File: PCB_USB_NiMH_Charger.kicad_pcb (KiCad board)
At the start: 2 copper layers, 94.9 x 72 mm, 61 parts, among them J1 USB_C_Receptacle_Simple, J2 Conn_02x01, Q1 2SA1015, Q2 2SC2458, Q3 2SB834, Q4 2SC2458, Q5 2SB834, Q6 2SC2458, Q7 2SB834, Q8 2SC2458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

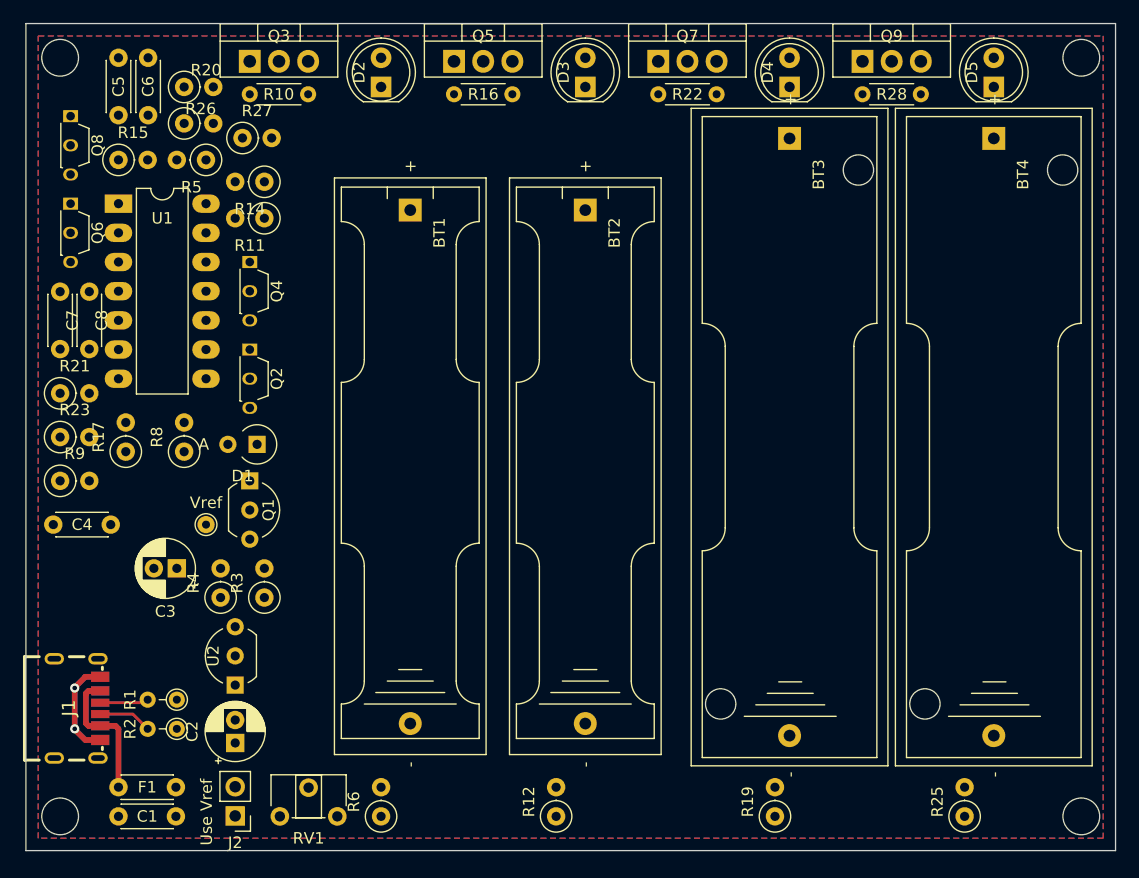
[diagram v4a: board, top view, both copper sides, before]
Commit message: Update to rev. 3
* LED を低消費電力版に変更し、LM339 で直接駆動するように変更。
  - 2SC1815 (2SC2458) を削除。
  - プルアップ抵抗を削除。
  - 680Ω を 2KΩ に変更。
* 10μF 電解コンデンサーを積層セラミックコンデンサーに変更。
* 2SB834 を裏面に配置。
* USB コネクタのフットプリントに間違いがあったのを修正。
  (取り付け穴が空いていなかったのを修正。)
* 配線を完了。
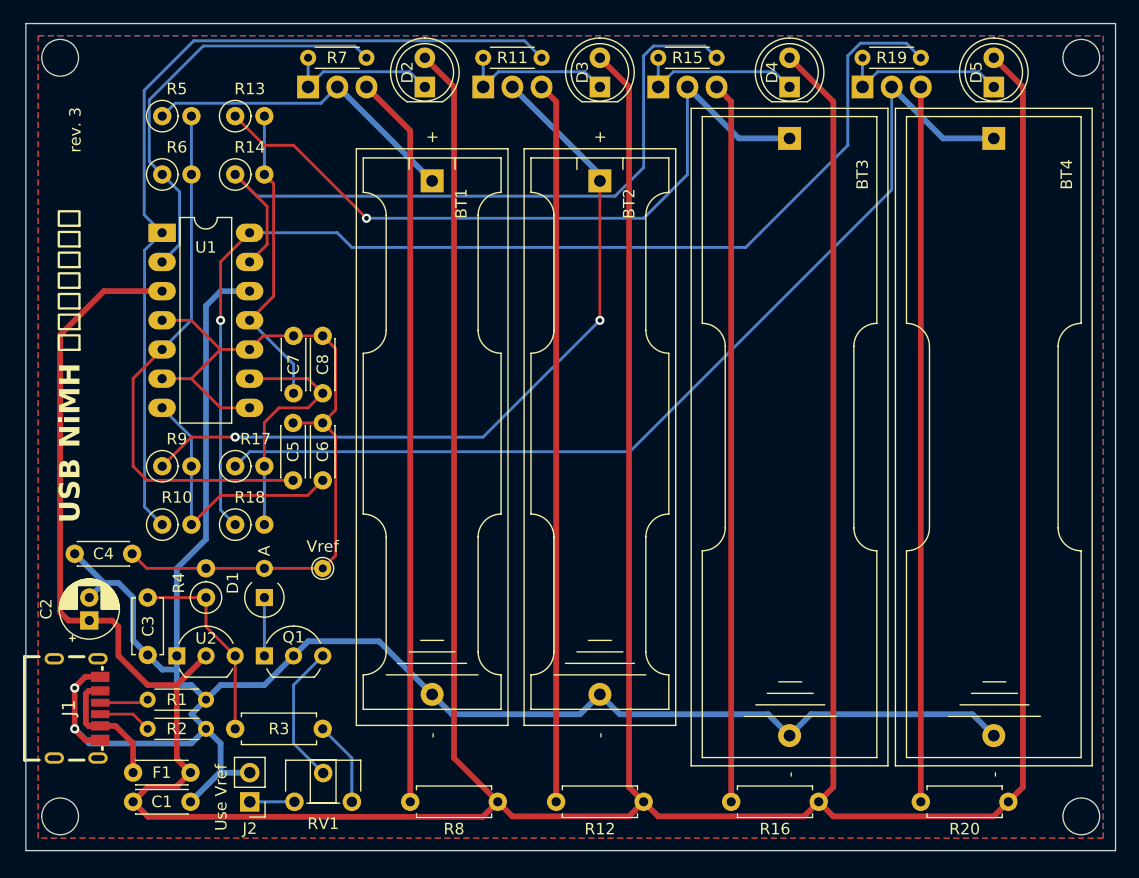
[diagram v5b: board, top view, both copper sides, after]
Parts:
- removed the Q2 at (44.5, 83.8)
- removed the Q4 at (44.5, 76.2)
- removed Q6, Q8: 2SC2458, Package_TO_SOT_THT:TO-92S_Wide
- removed the R11 at (45.7, 72.4)
- removed the R15 at (33.0, 67.3)
- removed the R20 at (38.7, 61.0)
- removed R21, R23, R27: 10k, Resistor_THT:R_Axial_DIN0207_L6.3mm_D2.5mm_P2.54mm_Vertical
- removed R26: 1M, Resistor_THT:R_Axial_DIN0207_L6.3mm_D2.5mm_P2.54mm_Vertical
- removed the R8 at (38.7, 92.7)
- added R13: 10k, Resistor_THT:R_Axial_DIN0207_L6.3mm_D2.5mm_P2.54mm_Vertical, F.Cu at (43.2, 63.5)
- added R14: 1M, Resistor_THT:R_Axial_DIN0207_L6.3mm_D2.5mm_P2.54mm_Vertical, F.Cu at (43.2, 68.6)
- added R18: 1M, Resistor_THT:R_Axial_DIN0207_L6.3mm_D2.5mm_P2.54mm_Vertical, F.Cu at (43.2, 99.1)
- added R6: 1M, Resistor_THT:R_Axial_DIN0207_L6.3mm_D2.5mm_P2.54mm_Vertical, F.Cu at (36.8, 68.6)
- C3: footprint Capacitor_THT:CP_Radial_D5.0mm_P2.00mm -> Capacitor_THT:C_Disc_D4.7mm_W2.5mm_P5.00mm
- D1: value 11EQS04 -> 11EQS03L
- Q2: renamed from Q3; footprint Package_TO_SOT_THT:TO-220-3_Vertical -> Package_TO_SOT_THT:TO-220-3_Horizontal_TabDown; moved to B.Cu
- Q3: renamed from Q5; footprint Package_TO_SOT_THT:TO-220-3_Vertical -> Package_TO_SOT_THT:TO-220-3_Horizontal_TabDown; moved to B.Cu
- Q4: renamed from Q7; footprint Package_TO_SOT_THT:TO-220-3_Vertical -> Package_TO_SOT_THT:TO-220-3_Horizontal_TabDown; moved to B.Cu
- Q5: renamed from Q9; footprint Package_TO_SOT_THT:TO-220-3_Vertical -> Package_TO_SOT_THT:TO-220-3_Horizontal_TabDown; moved to B.Cu
- R1, R2: footprint Resistor_THT:R_Axial_DIN0204_L3.6mm_D1.6mm_P2.54mm_Vertical -> Resistor_THT:R_Axial_DIN0204_L3.6mm_D1.6mm_P5.08mm_Horizontal
- R11: renamed from R16; value 680 -> 2.2k
- R12, R3: footprint Resistor_THT:R_Axial_DIN0207_L6.3mm_D2.5mm_P2.54mm_Vertical -> Resistor_THT:R_Axial_DIN0207_L6.3mm_D2.5mm_P7.62mm_Horizontal
- R15: renamed from R22; value 680 -> 2.2k
- R16: renamed from R19; value 10 -> 5.6; footprint Resistor_THT:R_Axial_DIN0207_L6.3mm_D2.5mm_P2.54mm_Vertical -> Resistor_THT:R_Axial_DIN0207_L6.3mm_D2.5mm_P7.62mm_Horizontal
- R19: renamed from R28; value 680 -> 2.2k
- R20: renamed from R25; value 10 -> 5.6; footprint Resistor_THT:R_Axial_DIN0207_L6.3mm_D2.5mm_P2.54mm_Vertical -> Resistor_THT:R_Axial_DIN0207_L6.3mm_D2.5mm_P7.62mm_Horizontal
- R7: renamed from R10; value 680 -> 2.2k
- R8: renamed from R6; footprint Resistor_THT:R_Axial_DIN0207_L6.3mm_D2.5mm_P2.54mm_Vertical -> Resistor_THT:R_Axial_DIN0207_L6.3mm_D2.5mm_P7.62mm_Horizontal
- moved C5 35.2 mm to (48.2, 95.2)
- moved C6 35.2 mm to (50.8, 95.2)
- moved R10 31.1 mm to (36.8, 99.1), turned to 0 degrees
- moved C7 20.7 mm to (48.3, 87.6)
- moved C8 20.7 mm to (50.8, 87.6)
- moved C2 16.6 mm to (30.5, 107.4)
- moved Q1 15.3 mm to (45.7, 110.5), turned to 0 degrees
- moved D1 13.4 mm to (45.7, 105.4), turned to 90 degrees
- moved R3 12.5 mm to (50.8, 116.8), turned to 180 degrees
- moved TP1 10.9 mm to (50.8, 102.9)
- moved R8 10.2 mm to (66.0, 123.2), turned to 180 degrees
- moved R17 9.61 mm to (43.2, 94.0), turned to 0 degrees
- moved R9 8.98 mm to (36.8, 94.0)
- moved R12 7.73 mm to (78.7, 123.2), turned to 180 degrees
- moved R7 5.99 mm to (49.5, 58.4)
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- renumbered R14 to R10
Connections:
- C5 pad 1: Net-(U1A--) -> Net-(U1A-+)
- C6 pad 1: Net-(U1B--) -> Net-(U1B-+)
- C7 pad 1: Net-(U1C--) -> Net-(U1C-+)
- C7 pad 2: Net-(U1C-+) -> Vref
- C8 pad 1: Net-(U1D--) -> Net-(U1D-+)
- F1 pad 1: +5V -> /VBUS
- F1 pad 2: /VBUS -> +5V
- R10 pad 1: Net-(Q4-C) -> Net-(R10-Pad1)
- R10 pad 2: Net-(U1B--) -> Net-(U1B-+)
- R11 pad 2: Net-(Q4-C) -> Net-(R10-Pad1)
- R15 pad 2: Net-(Q6-C) -> Net-(R14-Pad1)
- R17 pad 1: Net-(BT3-+) -> Net-(BT4-+)
- R17 pad 2: Net-(U1C--) -> Net-(U1D-+)
- R19 pad 2: Net-(Q8-C) -> Net-(R18-Pad1)
- R3 pad 1: /+3.3V -> Net-(R3-Pad1)
- R3 pad 2: Net-(R3-Pad2) -> /+3.3V
- R5 pad 2: Net-(U1A--) -> Net-(U1A-+)
- R7 pad 2: Net-(Q2-C) -> Net-(R6-Pad1)
- R9 pad 1: +5V -> Net-(BT2-+)
- R9 pad 2: Net-(Q2-B) -> Net-(U1B-+)
- RV1 pad 3: Net-(R3-Pad2) -> Net-(R3-Pad1)
- U1 pad 1: Net-(Q4-B) -> Net-(R10-Pad1)
- U1 pad 10: Net-(U1C--) -> Vref
- U1 pad 13: Net-(Q6-B) -> Net-(R14-Pad1)
- U1 pad 14: Net-(Q8-B) -> Net-(R18-Pad1)
- U1 pad 2: Net-(Q2-B) -> Net-(R6-Pad1)
- U1 pad 4: Net-(U1A--) -> Vref
- U1 pad 5: Vref -> Net-(U1A-+)
- U1 pad 6: Net-(U1B--) -> Vref
- U1 pad 7: Vref -> Net-(U1B-+)
- U1 pad 8: Net-(U1D--) -> Vref
- U1 pad 9: Vref -> Net-(U1D-+)
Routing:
- net +5V: track 0.00 -> 414.1 mm
- net GND: track 8.86 -> 171.1 mm
- net Net-(R18-Pad1): track 0.00 -> 98.4 mm, vias 0 -> 1
- net Net-(BT4-+): track 0.00 -> 86.9 mm
- net Net-(R10-Pad1): track 0.00 -> 76.7 mm
- net Vref: track 0.00 -> 69.6 mm
- net Net-(BT2-+): track 0.00 -> 66.8 mm, vias 0 -> 2
- net Net-(Q2-E): track 0.00 -> 63.8 mm
- net Net-(R14-Pad1): track 0.00 -> 63.6 mm
- net Net-(BT3-+): track 0.00 -> 63.0 mm, vias 0 -> 1
- net Net-(Q3-E): track 0.00 -> 62.8 mm
- net Net-(Q4-E): track 0.00 -> 62.8 mm
- net Net-(Q5-E): track 0.00 -> 62.2 mm
- net Net-(U1A-+): track 0.00 -> 47.0 mm
- net Net-(R6-Pad1): track 0.00 -> 37.1 mm
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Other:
- board text added: "USB NiMH ゆっくり充電器"
- board text added: "rev. 3"

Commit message: 配線を調整
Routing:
- net Net-(R18-Pad1): track 98.4 -> 101.3 mm
- net Net-(Q1-B): track 12.3 -> 11.3 mm
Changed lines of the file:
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@@
     (property "ki_keywords" "Power PNP Transistor")
     (attr through_hole)
-    (fp_text reference "Q2" (at 3.81 20.828 180) (layer "B.SilkS")
+    (fp_text reference "Q2" (at 3.81 20.574 180) (layer "B.SilkS")
         (effects (font (size 1 1) (thickness 0.15)) (justify mirror))
     )
@@
   (segment (start 43.18 110.49) (end 43.18 116.84) (width 0.25) (layer "F.Cu") (net 15))
   (segment (start 43.18 110.49) (end 40.64 107.95) (width 0.25) (layer "F.Cu") (net 15))
-  (segment (start 48.26 118.11) (end 48.26 113.03) (width 0.25) (layer "B.Cu") (net 16))
-  (segment (start 50.84 120.69) (end 48.26 118.11) (width 0.25) (layer "B.Cu") (net 16))
-  (segment (start 48.26 113.03) (end 50.8 110.49) (width 0.25) (layer "B.Cu") (net 16))
-  (segment (start 54.61 72.39) (end 48.26 66.04) (width 0.25) (layer "F.Cu") (net 17))
-  (segment (start 45.72 66.04) (end 43.18 63.5) (width 0.25) (layer "F.Cu") (net 17))
-  (segment (start 48.26 66.04) (end 45.72 66.04) (width 0.25) (layer "F.Cu") (net 17))
-  (via (at 54.61 72.39) (size 0.8) (drill 0.4) (layers "F.Cu" "B.Cu") (net 17))
+  (segment (start 49.53 111.76) (end 50.8 110.49) (width 0.25) (layer "B.Cu") (net 16))
+  (segment (start 49.53 111.76) (end 49.53 119.38) (width 0.25) (layer "B.Cu") (net 16))
+  (segment (start 50.84 120.69) (end 49.53 119.38) (width 0.25) (layer "B.Cu") (net 16))
+  (segment (start 43.18 63.5) (end 52.07 72.39) (width 0.25) (layer "F.Cu") (net 17))
+  (via (at 52.07 72.39) (size 0.8) (drill 0.4) (layers "F.Cu" "B.Cu") (net 17))
   (segment (start 91.44 65.44) (end 87.03 65.44) (width 0.5) (layer "B.Cu") (net 17))
   (segment (start 54.61 72.39) (end 78.74 72.39) (width 0.25) (layer "B.Cu") (net 17))
   (segment (start 82.55 68.58) (end 82.55 60.96) (width 0.25) (layer "B.Cu") (net 17))
   (segment (start 87.03 65.44) (end 82.55 60.96) (width 0.5) (layer "B.Cu") (net 17))
+  (segment (start 52.07 72.39) (end 54.61 72.39) (width 0.25) (layer "B.Cu") (net 17))
   (segment (start 78.74 72.39) (end 82.55 68.58) (width 0.25) (layer "B.Cu") (net 17))
   (segment (start 77.505 92.745) (end 77.47 92.71) (width 0.25) (layer "B.Cu") (net 18))
@@
   (segment (start 45.96 74.67) (end 44.435 76.195) (width 0.25) (layer "F.Cu") (net 26))
   (segment (start 45.96 71.36) (end 45.96 74.67) (width 0.25) (layer "F.Cu") (net 26))
-  (segment (start 78.74 66.04) (end 78.74 67.98) (width 0.25) (layer "B.Cu") (net 26))
-  (segment (start 78.74 58.42) (end 78.7325 58.4275) (width 0.25) (layer "B.Cu") (net 26))
-  (segment (start 85.09 58.42) (end 84.065 57.395) (width 0.25) (layer "B.Cu") (net 26))
-  (segment (start 78.7325 58.4275) (end 78.7325 66.0325) (width 0.25) (layer "B.Cu") (net 26))
-  (segment (start 78.74 58.240431) (end 78.74 58.42) (width 0.25) (layer "B.Cu") (net 26))
-  (segment (start 78.74 67.98) (end 76.255 70.465) (width 0.25) (layer "B.Cu") (net 26))
-  (segment (start 45.065 70.465) (end 43.18 68.58) (width 0.25) (layer "B.Cu") (net 26))
-  (segment (start 84.065 57.395) (end 79.585431 57.395) (width 0.25) (layer "B.Cu") (net 26))
-  (segment (start 76.255 70.465) (end 45.065 70.465) (width 0.25) (layer "B.Cu") (net 26))
-  (segment (start 78.7325 66.0325) (end 78.74 66.04) (width 0.25) (layer "B.Cu") (net 26))
-  (segment (start 79.585431 57.395) (end 78.74 58.240431) (width 0.25) (layer "B.Cu") (net 26))
+  (segment (start 84.065 57.395) (end 85.09 58.42) (width 0.25) (layer "B.Cu") (net 26))
+  (segment (start 79.585431 57.395) (end 84.065 57.395) (width 0.25) (layer "B.Cu") (net 26))
+  (segment (start 45.065 70.465) (end 76.255 70.465) (width 0.25) (layer "B.Cu") (net 26))
+  (segment (start 78.7325 66.0325) (end 78.7325 58.247931) (width 0.25) (layer "B.Cu") (net 26))
+  (segment (start 78.7325 58.247931) (end 79.585431 57.395) (width 0.25) (layer "B.Cu") (net 26))
+  (segment (start 78.74 67.98) (end 78.74 66.04) (width 0.25) (layer "B.Cu") (net 26))
+  (segment (start 76.255 70.465) (end 78.74 67.98) (width 0.25) (layer "B.Cu") (net 26))
+  (segment (start 43.18 68.58) (end 45.065 70.465) (width 0.25) (layer "B.Cu") (net 26))
+  (segment (start 78.74 66.04) (end 78.7325 66.0325) (width 0.25) (layer "B.Cu") (net 26))
   (segment (start 58.42 64.77) (end 54.61 60.96) (width 0.5) (layer "F.Cu") (net 27))
   (segment (start 58.42 123.19) (end 58.42 64.77) (width 0.5) (layer "F.Cu") (net 27))
@@
   (segment (start 41.91 76.18) (end 44.435 73.655) (width 0.25) (layer "F.Cu") (net 31))
   (via (at 41.91 81.28) (size 0.8) (drill 0.4) (layers "F.Cu" "B.Cu") (net 31))
-  (segment (start 88.905 73.655) (end 96.52 66.04) (width 0.25) (layer "B.Cu") (net 31))
-  (segment (start 87.63 74.93) (end 88.9 73.66) (width 0.25) (layer "B.Cu") (net 31))
-  (segment (start 52.065 73.655) (end 53.34 74.93) (width 0.25) (layer "B.Cu") (net 31))
-  (segment (start 96.52 66.04) (end 96.5125 66.0325) (width 0.25) (layer "B.Cu") (net 31))
-  (segment (start 53.34 74.93) (end 87.63 74.93) (width 0.25) (layer "B.Cu") (net 31))
-  (segment (start 96.5125 58.247931) (end 97.610431 57.15) (width 0.25) (layer "B.Cu") (net 31))
-  (segment (start 101.6 57.15) (end 102.87 58.42) (width 0.25) (layer "B.Cu") (net 31))
-  (segment (start 44.435 73.655) (end 52.065 73.655) (width 0.25) (layer "B.Cu") (net 31))
+  (segment (start 87.63 74.93) (end 96.5125 66.0475) (width 0.25) (layer "B.Cu") (net 31))
+  (segment (start 101.845 57.395) (end 97.365431 57.395) (width 0.25) (layer "B.Cu") (net 31))
+  (segment (start 44.435 73.655) (end 50.8 73.655) (width 0.25) (layer "B.Cu") (net 31))
+  (segment (start 50.8 73.66) (end 50.8 73.655) (width 0.25) (layer "B.Cu") (net 31))
+  (segment (start 102.87 58.42) (end 101.845 57.395) (width 0.25) (layer "B.Cu") (net 31))
+  (segment (start 96.5125 66.0475) (end 96.5125 64.77) (width 0.25) (layer "B.Cu") (net 31))
+  (segment (start 97.365431 57.395) (end 96.5125 58.247931) (width 0.25) (layer "B.Cu") (net 31))
+  (segment (start 96.5125 58.247931) (end 96.5125 64.77) (width 0.25) (layer "B.Cu") (net 31))
+  (segment (start 50.795 73.655) (end 52.07 74.93) (width 0.25) (layer "B.Cu") (net 31))
+  (segment (start 52.07 74.93) (end 87.63 74.93) (width 0.25) (layer "B.Cu") (net 31))
+  (segment (start 96.5125 64.77) (end 96.5125 66.0325) (width 0.25) (layer "B.Cu") (net 31))
   (segment (start 41.91 97.79) (end 41.91 81.28) (width 0.25) (layer "B.Cu") (net 31))
-  (segment (start 97.610431 57.15) (end 101.6 57.15) (width 0.25) (layer "B.Cu") (net 31))
-  (segment (start 96.5125 66.0325) (end 96.5125 58.247931) (width 0.25) (layer "B.Cu") (net 31))
+  (segment (start 96.5125 66.0325) (end 96.52 66.04) (width 0.25) (layer "B.Cu") (net 31))
+  (segment (start 52.07 74.93) (end 50.8 73.66) (width 0.25) (layer "B.Cu") (net 31))
   (segment (start 43.18 99.06) (end 41.91 97.79) (width 0.25) (layer "B.Cu") (net 31))
   (segment (start 53.34 119.38) (end 50.8 116.84) (width 0.25) (layer "B.Cu") (net 32))

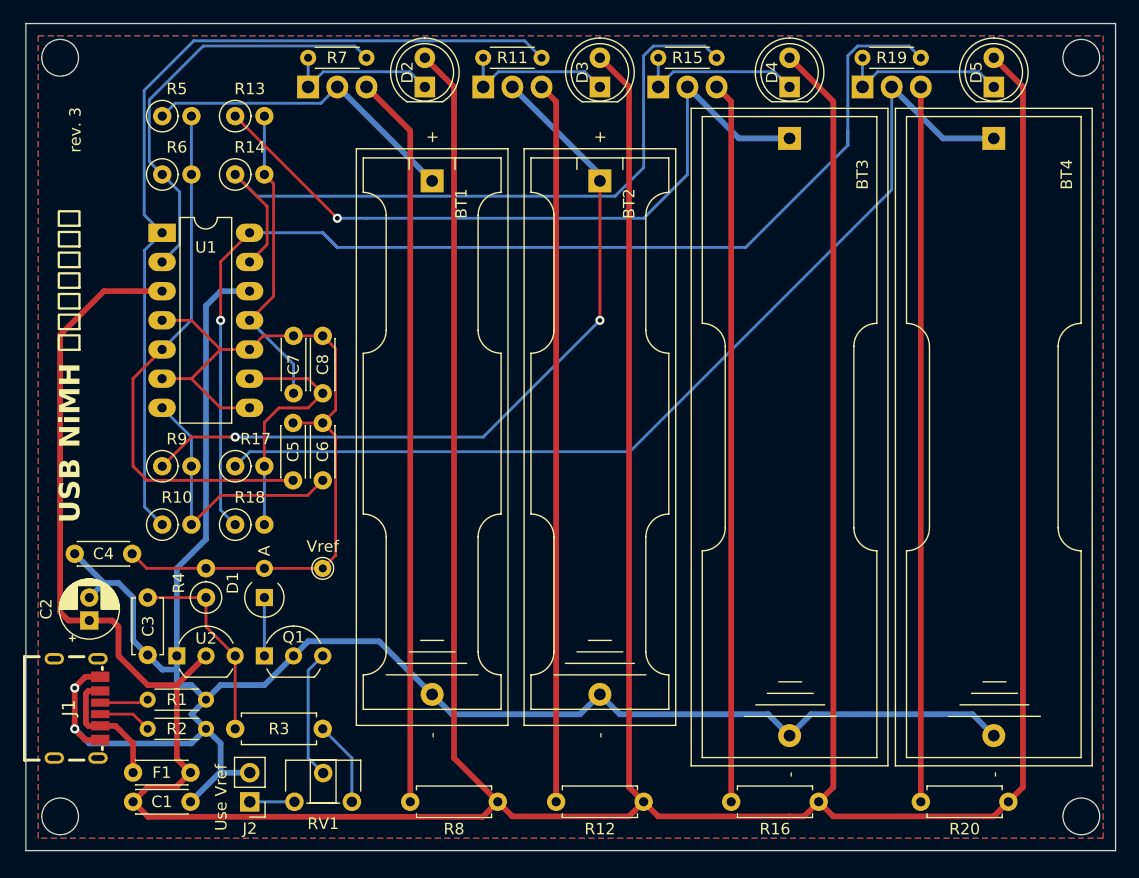
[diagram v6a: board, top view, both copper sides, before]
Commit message: 微調整
* 配線を調整。
* BT1, BT2のパッド位置を調整。(マイナス側を0.2mm外側へ移動。)
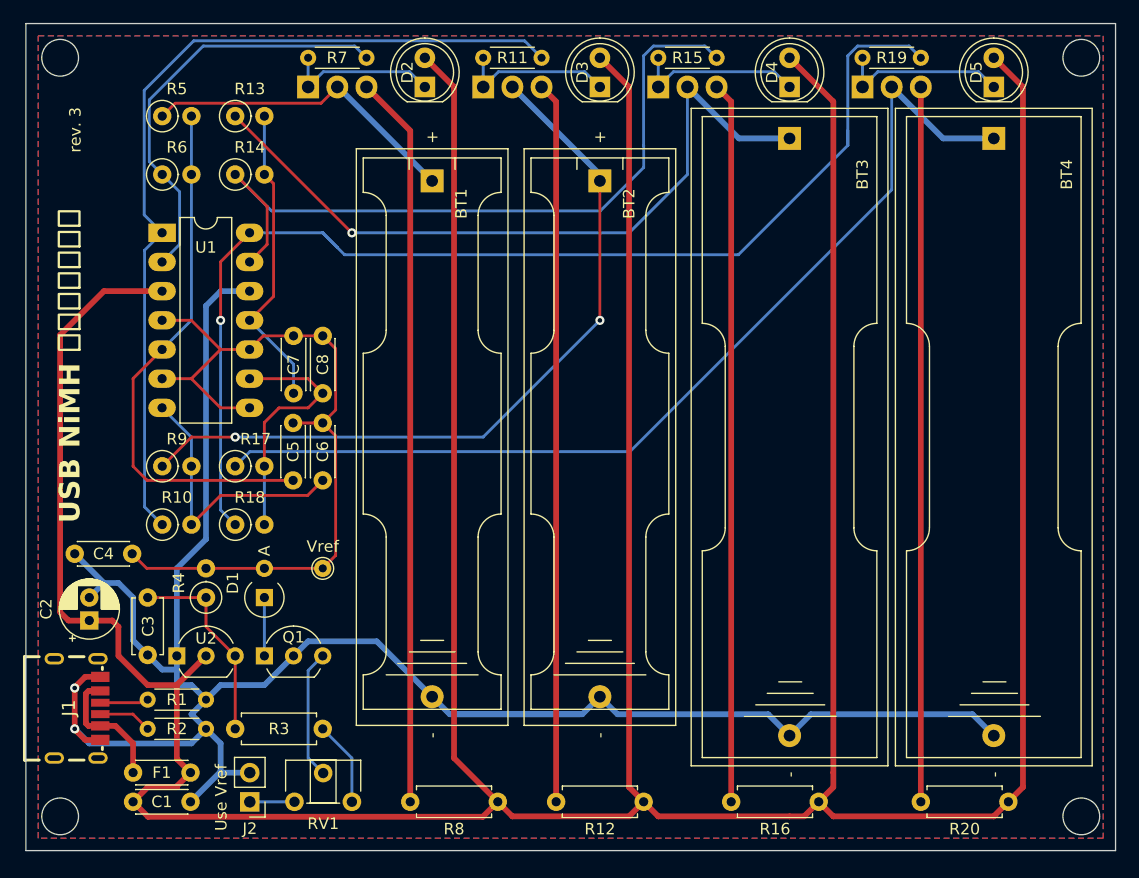
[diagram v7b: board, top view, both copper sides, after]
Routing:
- net GND: track 171.1 -> 182.1 mm
- net Net-(R14-Pad1): track 63.6 -> 64.7 mm
- net Net-(BT3-+): track 63.0 -> 64.0 mm
- net Net-(R18-Pad1): track 101.3 -> 101.8 mm

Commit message: 配線を調整
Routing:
- net Net-(R14-Pad1): track 64.7 -> 64.1 mm
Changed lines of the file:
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@@
   (segment (start 49.53 88.9) (end 50.8 87.63) (width 0.25) (layer "F.Cu") (net 25))
   (segment (start 45.72 99.06) (end 45.72 93.98) (width 0.25) (layer "B.Cu") (net 25))
-  (segment (start 43.18 68.58) (end 45.96 71.36) (width 0.25) (layer "F.Cu") (net 26))
-  (segment (start 45.96 74.67) (end 44.435 76.195) (width 0.25) (layer "F.Cu") (net 26))
-  (segment (start 45.96 71.36) (end 45.96 74.67) (width 0.25) (layer "F.Cu") (net 26))
   (segment (start 78.7325 58.247931) (end 78.7325 66.0325) (width 0.25) (layer "B.Cu") (net 26))
   (segment (start 78.7325 66.0325) (end 78.74 66.04) (width 0.25) (layer "B.Cu") (net 26))
+  (segment (start 42.380001 74.140001) (end 44.435 76.195) (width 0.25) (layer "B.Cu") (net 26))
   (segment (start 74.965 71.755) (end 46.355 71.755) (width 0.25) (layer "B.Cu") (net 26))
   (segment (start 78.74 67.98) (end 74.965 71.755) (width 0.25) (layer "B.Cu") (net 26))
   (segment (start 78.74 66.04) (end 78.74 67.98) (width 0.25) (layer "B.Cu") (net 26))
+  (segment (start 42.380001 69.379999) (end 42.380001 74.140001) (width 0.25) (layer "B.Cu") (net 26))
   (segment (start 79.585431 57.395) (end 78.7325 58.247931) (width 0.25) (layer "B.Cu") (net 26))
+  (segment (start 43.18 68.58) (end 42.380001 69.379999) (width 0.25) (layer "B.Cu") (net 26))
   (segment (start 84.065 57.395) (end 79.585431 57.395) (width 0.25) (layer "B.Cu") (net 26))
   (segment (start 46.355 71.755) (end 43.18 68.58) (width 0.25) (layer "B.Cu") (net 26))
